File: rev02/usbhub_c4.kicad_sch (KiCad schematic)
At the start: 119 parts, among them J1 5077CR-16SMC2, J2 Conn_01x01, J3 Conn_01x01, J4 Conn_01x01, J5 5077CR-16SMC2, J6 5077CR-16SMC2, J7 5077CR-16SMC2, J8 5077CR-16SMC2, Q1 BSS138, Q2 BSS138, Q3 BSS138, Q4 BSS138, SW1 SKRPACE010, U1 LM3670MF-3.3, U2 μPD720115, U3 TPS25821, U4 TPS25821, U5 TPS25821, U6 TPS25821, Y1 24MHz

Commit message: シンプル版追加
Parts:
- removed C1: 4.7uF, Capacitor_SMD:C_1206_3216Metric, symbol Device:C_Small
- removed C17, C18, C19, C2, C22, C23, C24, C27, C28, C29, C3, C32, C33, C34: 47uF, Capacitor_SMD:C_1210_3225Metric, symbol Device:C_Small
- removed C4: 0.1uF, Capacitor_SMD:C_0603_1608Metric, symbol Device:C_Small
- removed D3: Green, LED_SMD:LED_0603_1608Metric, symbol Device:LED_Small_Filled
- removed J2, J3, J4: Conn_01x01, _platinumegg:PinHeader_1x01_P2.54mm_Vertical, symbol Connector_Generic:Conn_01x01
- removed L1: 10uH, _platinumegg:IND_LQH5BPN100M38L, symbol Device:L_Small
- removed L2: 1uH, Inductor_SMD:L_1210_3225Metric, symbol Device:L_Small
- removed Q1, Q2, Q3, Q4: BSS138, _platinumegg:SOT-23, symbol Transistor_FET:BSS138
- removed R19: 10kΩ, Resistor_SMD:R_0402_1005Metric, symbol Device:R_Small
- removed R22, R27, R32, R37: 100kΩ, Resistor_SMD:R_0603_1608Metric, symbol Device:R_Small
- removed R4: 47kΩ, Resistor_SMD:R_0603_1608Metric, symbol Device:R_Small
- removed U1: LM3670MF-3.3, Package_TO_SOT_SMD:TSOT-23-5, symbol Regulator_Switching:LM3670MF
- added C22, C23, C24, C27: 150uF, Capacitor_THT:CP_Radial_D6.3mm_P2.50mm, symbol Device:C_Polarized_Small
- added U1, U7, U8, U9: TC7SH00FU, Package_TO_SOT_SMD:SOT-353_SC-70-5, symbol _platinumegg:TC7SH00FU
- C14, C8: footprint Capacitor_SMD:C_0402_1005Metric -> Capacitor_SMD:C_1206_3216Metric
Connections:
- net V_{BUS}M is gone; now on net VCC_{5V}: U2.3 (V_{BUS}M)
- net 3V3: now also U2.5 (V_{DD}33_{OUT})
- net GND: now also C22.2, C23.2, C24.2, C27.2, U1.3 (GND), U7.3 (GND), U8.3 (GND), U9.3 (GND); no longer U2.4 (V_{DD}50_{IN})
- net VCC_{5V}: now also U2.4 (V_{DD}50_{IN}), C22.1, C23.1, C24.1, C27.1, U1.5 (VCC), U7.5 (VCC), U8.5 (VCC), U9.5 (VCC)
- net ~{PPON}_{1}: now also U7.2
- net ~{PPON}_{2}: now also U1.2
- net ~{PPON}_{3}: now also U8.2
- net ~{PPON}_{4}: now also U9.2
- net at U4.4 (EN): now also U1.4
- net at U6.4 (EN): now also U9.4
- net at U3.4 (EN): now also U7.4
- net at U5.4 (EN): now also U8.4
- no-connect marks 7 -> 10
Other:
- moved on the sheet: C20, C25, C30, C35

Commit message: ダウンストリームポートキャパシタを高分子コンデンサに変更
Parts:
- added J2: Conn_01x02, Connector_JST:JST_PH_B2B-PH-K_1x02_P2.00mm_Vertical, symbol Connector_Generic:Conn_01x02
- added R10, R20: 15kΩ, Resistor_SMD:R_0603_1608Metric, symbol Device:R_Small
- added R11, R19: 10kΩ, Resistor_SMD:R_0603_1608Metric, symbol Device:R_Small
- D12: renamed from D13; value WarmWhite -> Aqua
- D13: renamed from D15; value WarmWhite -> Aqua
- D8: renamed from D9; value WarmWhite -> Aqua
- D9: renamed from D11; value WarmWhite -> Aqua
- U1: renamed from U2; footprint Package_DFN_QFN:QFN-40-1EP_6x6mm_P0.5mm_EP4.6x4.6mm -> _platinumegg:QFN-40-1EP_6x6mm_P0.5mm_EP4.6x4.6mm
- renumbered C5 to C1, C11 to C10, C12 to C11, C13 to C12, C22 to C13, C23 to C14, C20 to C15, C25 to C16, C21 to C17, C26 to C18, C24 to C19, C6 to C2, C27 to C20, C30 to C21, C35 to C22, C31 to C23, C36 to C24, C7 to C3, C8 to C4, C14 to C5, C9 to C6, C15 to C7, C10 to C8, C16 to C9, D12 to D11, D16 to D15, D4 to D2, D5 to D3, D6 to D4, D2 to D5, D7 to D6, D8 to D7, J5 to J3, J6 to J4, J7 to J5, J8 to J6, R5 to R1, R8 to R12, R12 to R13, R16 to R14, R3 to R15, R9 to R16, R13 to R17, R17 to R18, R1 to R2, R10 to R22, R14 to R23, R18 to R24, R21 to R25, R23 to R27, R24 to R29, R2 to R3, R29 to R30, R25 to R31, R30 to R32, R31 to R33, R36 to R34, R33 to R35, R38 to R36, R34 to R37, R39 to R38, R35 to R39, R20 to R4, R6 to R5, R7 to R6, R11 to R7, R15 to R8, U7 to U2, U1 to U3, U3 to U4, U4 to U5, U8 to U6, U9 to U7, U5 to U8, U6 to U9
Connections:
- net GND: now also J2.2 (Pin_2), R10.2, R20.2
- net VCC_{5V}: now also J2.1 (Pin_1), R11.1, R19.1; no longer U1.2 (LPwrM), U1.3 (V_{BUS}M)
- new net LPrwM: R10.1, R11.2, U1.2 (LPwrM)
- new net V_{BUS}M: R19.2, R20.1, U1.3 (V_{BUS}M)
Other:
- moved on the sheet: C10, C11, C12, C13, C14, C15, C16, C17, C18, C19, C20, C21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

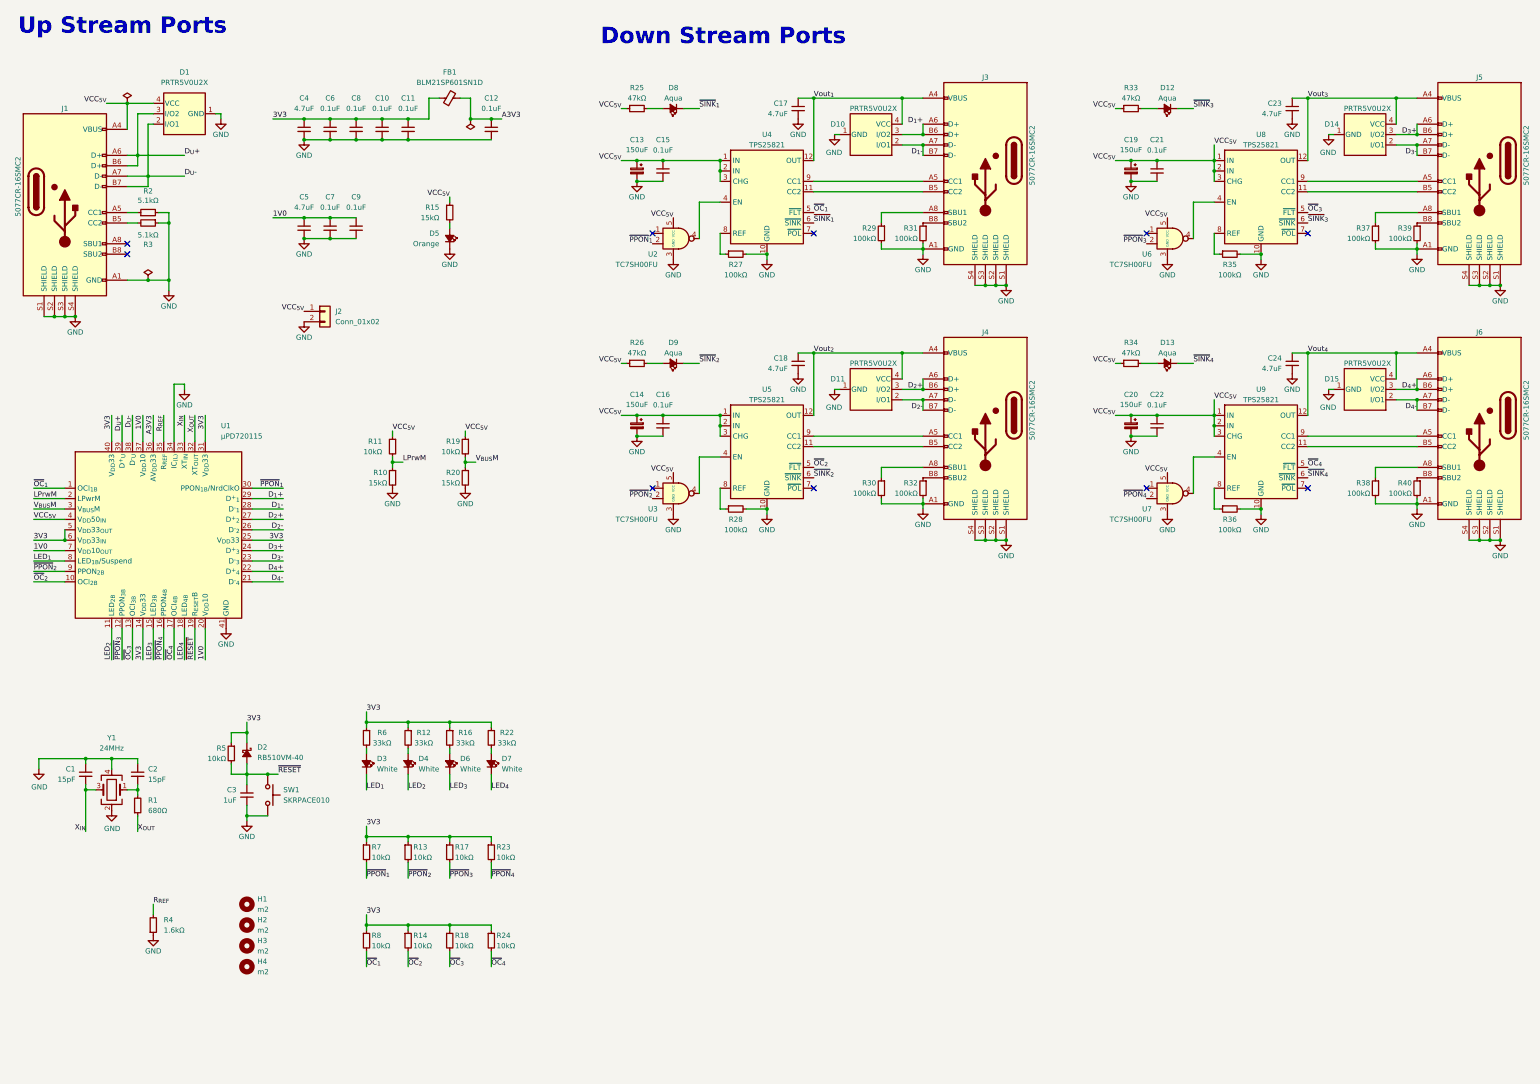
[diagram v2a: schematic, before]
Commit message: ダウンストリームポートキャパシタをコールドになる位置に変更
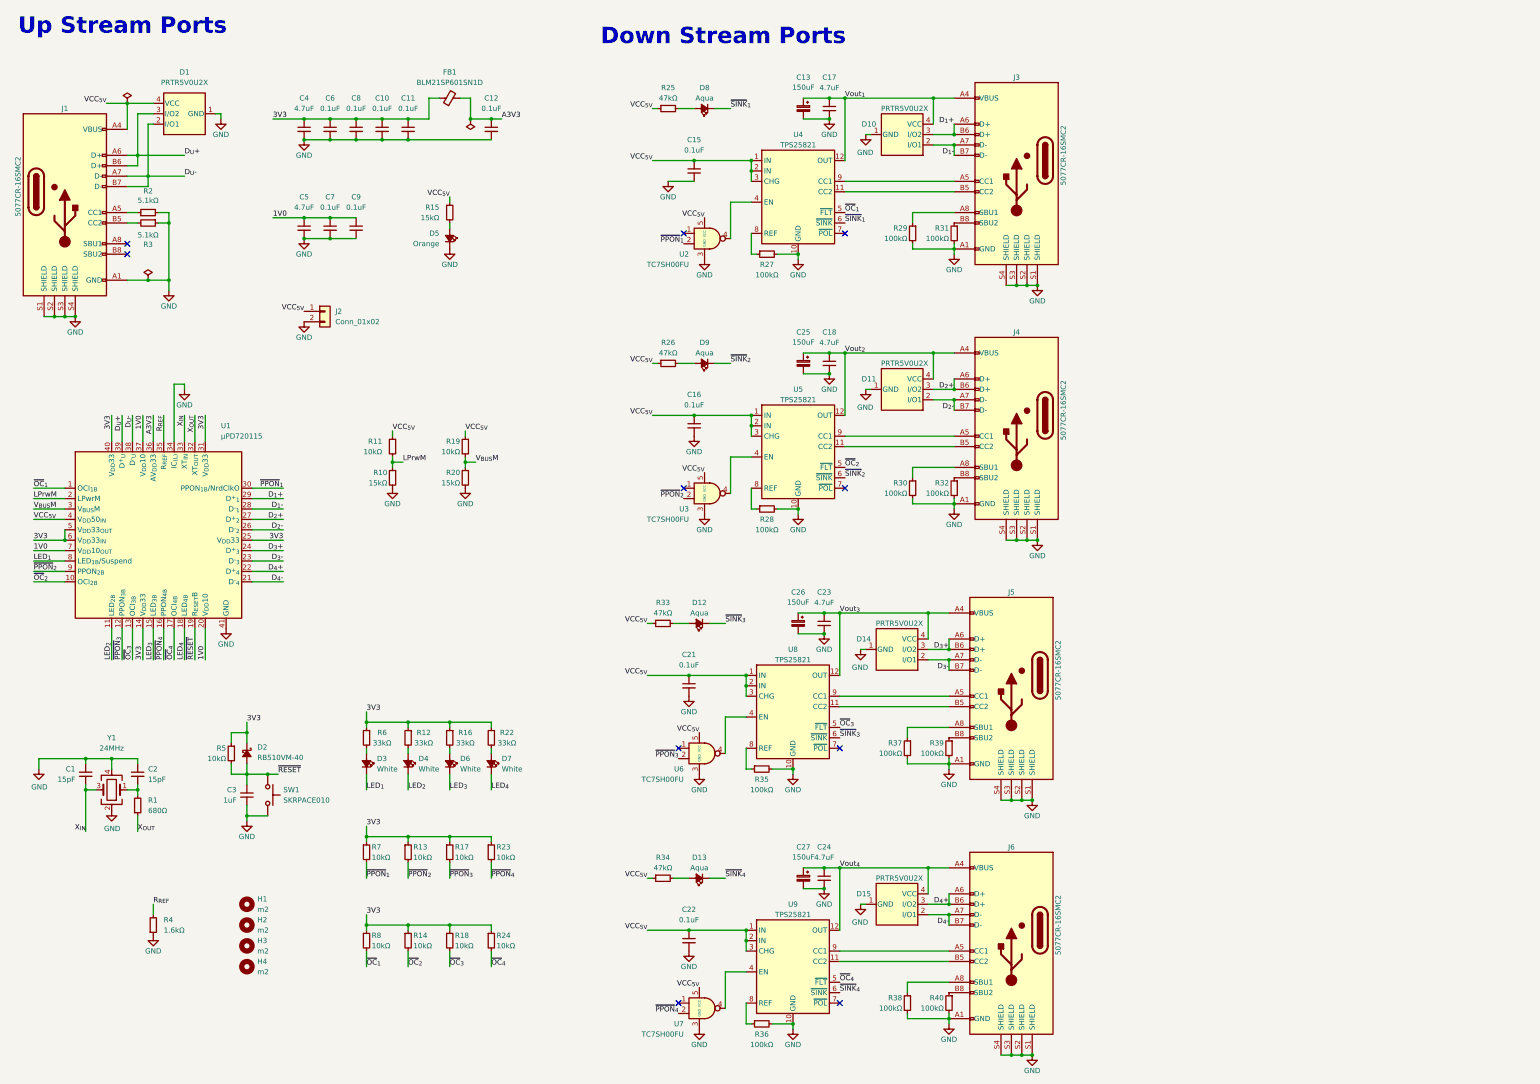
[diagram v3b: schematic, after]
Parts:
- removed C14, C19, C20: 150uF, Capacitor_THT:CP_Radial_D6.3mm_P2.50mm, symbol Device:C_Polarized_Small
- added C25, C26, C27: 150uF, Capacitor_THT:CP_Radial_D6.3mm_P2.50mm, symbol Device:C_Polarized_Small
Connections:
- net GND: now also C25.2, C26.2, C27.2
- net VCC_{5V}: no longer C13.1
- net Vout_{1}: now also C13.1
- net Vout_{2}: now also C25.1
- net Vout_{3}: now also C26.1
- net Vout_{4}: now also C27.1
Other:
- moved on the sheet: C13, C15, C16, C17, C18, C21, C22, C23, C24, D10, D11, D12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

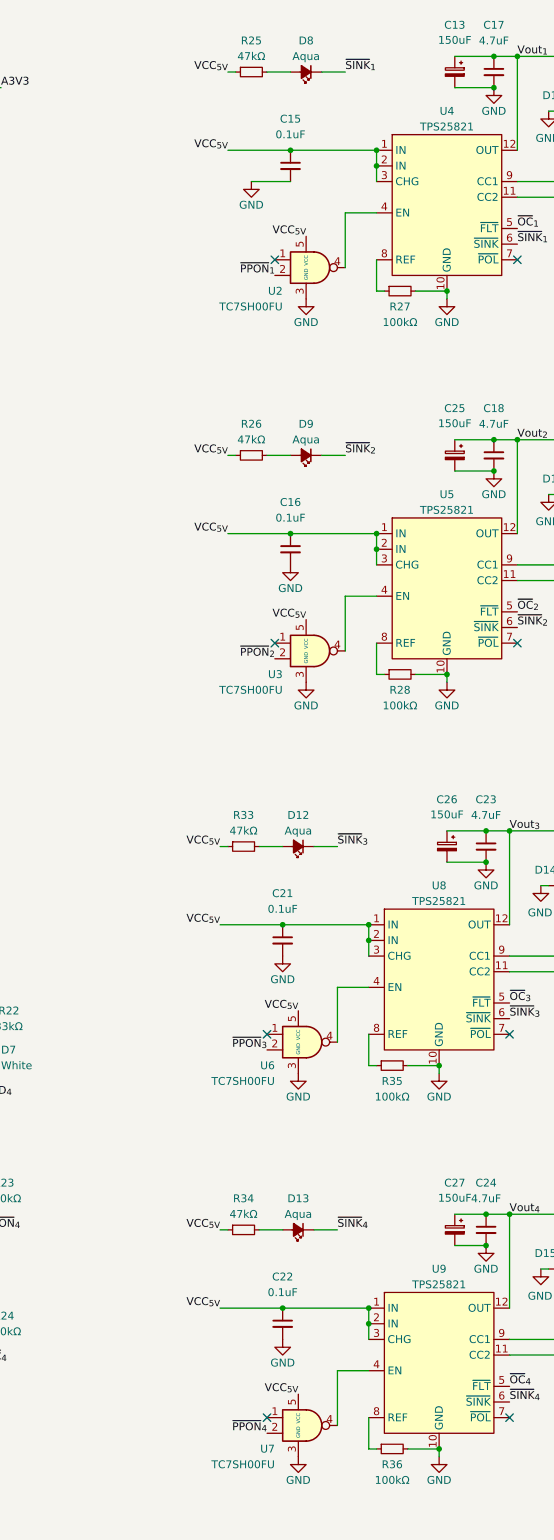
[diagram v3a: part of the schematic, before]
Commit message: Add teardrops and update routing in USB hub PCB
Added teardrops to multiple pads and vias in rev02/usbhub_c4.kicad_pcb for improved manufacturability. Updated several net routings, modified some arc and segment connections, and made minor schematic and layout adjustments. Removed fabrication-toolkit-options.json files from rev01 and rev02, updated .gitignore to exclude production folders, and incremented PCB revision text to 0.3.1 with updated date.
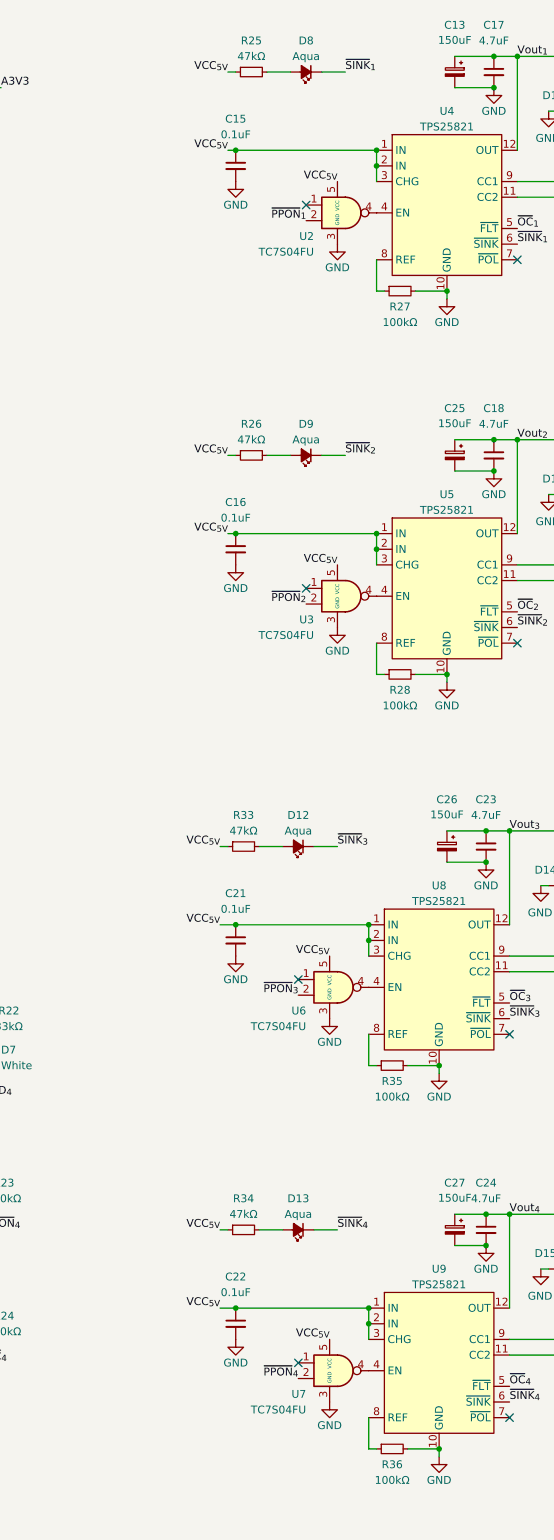
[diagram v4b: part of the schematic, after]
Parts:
- U2, U3, U6, U7: value TC7SH00FU -> TC7S04FU
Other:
- moved on the sheet: C15, C16, C21, C22, U2, U3, U6, U7
